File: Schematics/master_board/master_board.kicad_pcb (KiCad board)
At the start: 2 copper layers, 70 parts, among them J1 2x5x1.27mm, J10 Conn_01x06_Male, J11 Conn_01x06_Male, J12 Conn_01x06_Male, J13 Conn_01x06_Male, J14 Conn_01x06_Male, J15 Conn_01x06_Male, J16 Conn_01x06_Male, J17 Conn_01x06_Male, J18 Conn_01x06_Male, J19 Conn_01x06_Male, J2 USB_C_Receptacle_USB2.0, J20 Conn_01x06_Male, J21 Conn_01x06_Male, J22 Conn_01x06_Male, J23 Conn_01x06_Male, J24 Conn_01x06_Male, J25 Conn_01x06_Male, J26 Conn_01x06_Male, J3 Conn_01x01_Female, J4 Conn_01x01_Female, J5 Conn_01x01_Female, J6 Conn_01x01_Female, J7 Conn_01x06_Male, J8 Conn_01x06_Male, J9 Conn_01x06_Male, SW1 SW_Push, SW2 SW_Push, SW3 SW_Push, U1 NCP1117-3.3_SOT223, U2 RP2040, U3 W25Q16JVSSIQ, U4 74HCT154PW,118, U5 74HCT154PW,118, Y1 ABLS-12.000MHZ-B4-T

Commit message: Finalize master board placement, begin routing
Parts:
- added H1: MountingHole, MountingHole:MountingHole_3.2mm_M3, F.Cu at (22.0, 23.0)
- added H2: MountingHole, MountingHole:MountingHole_3.2mm_M3, F.Cu at (22.0, 169.0)
- added H3: MountingHole, MountingHole:MountingHole_3.2mm_M3, F.Cu at (168.0, 23.0)
- added H4: MountingHole, MountingHole:MountingHole_3.2mm_M3, F.Cu at (168.0, 169.0)
- moved U4 186.9 mm to (50.0, 40.0)
- moved U5 180.4 mm to (70.0, 40.0)
- moved J10 179.3 mm to (32.0, 146.8)
- moved J9 172.4 mm to (32.0, 115.2)
- moved J7 169.8 mm to (32.0, 52.2)
- moved R13 169.3 mm to (62.9, 21.9), turned to -90 degrees
- moved J8 169.2 mm to (32.0, 83.8)
- moved R15 165.0 mm to (63.6, 21.9), turned to 90 degrees
- moved C17 165.0 mm to (74.3, 21.7), turned to 90 degrees
- moved J14 164.7 mm to (63.5, 146.8)
- moved U3 162.8 mm to (68.9, 24.1)
- moved J13 157.3 mm to (63.5, 115.2)
- moved J11 154.4 mm to (63.5, 52.2)
- moved J12 153.7 mm to (63.5, 83.8)
- moved D1 151.2 mm to (82.7, 28.4), turned to 90 degrees
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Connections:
- net Net-(C13-Pad2) renamed /XTAL_OUT_PRE
- net Net-(J1-Pad10) renamed /CONN_RUN_N
- net Net-(J1-Pad2) renamed /CONN_SWDIO
- net Net-(J1-Pad4) renamed /CONN_SWCLK
- net Net-(J2-PadA5) renamed /CC1_USB
- net Net-(J2-PadB5) renamed /CC2_USB
- net Net-(J3-Pad1) renamed /CONN_HAP_L
- net Net-(J6-Pad1) renamed /CONN_HAP_R
- U2 pad 28: /GPIO17 -> /RESCAN_N
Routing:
- net /USB_D+: track 0.00 -> 32.3 mm, vias 0 -> 2
- net /USB_D-: track 0.00 -> 30.9 mm
- net /XTAL_OUT_PRE: track 0.00 -> 7.64 mm
- net /USB_D+I: track 0.00 -> 2.78 mm
- net /USB_D-I: track 0.00 -> 2.66 mm
- net +3V3: track 0.00 -> 1.85 mm
- net +1V1: track 0.00 -> 1.57 mm
- added copper zone on F.Cu, net +3V3
- added copper zone on B.Cu, net GND
- added copper zone on F.Cu, net GND
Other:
- board outline added: 156 x 156 mm

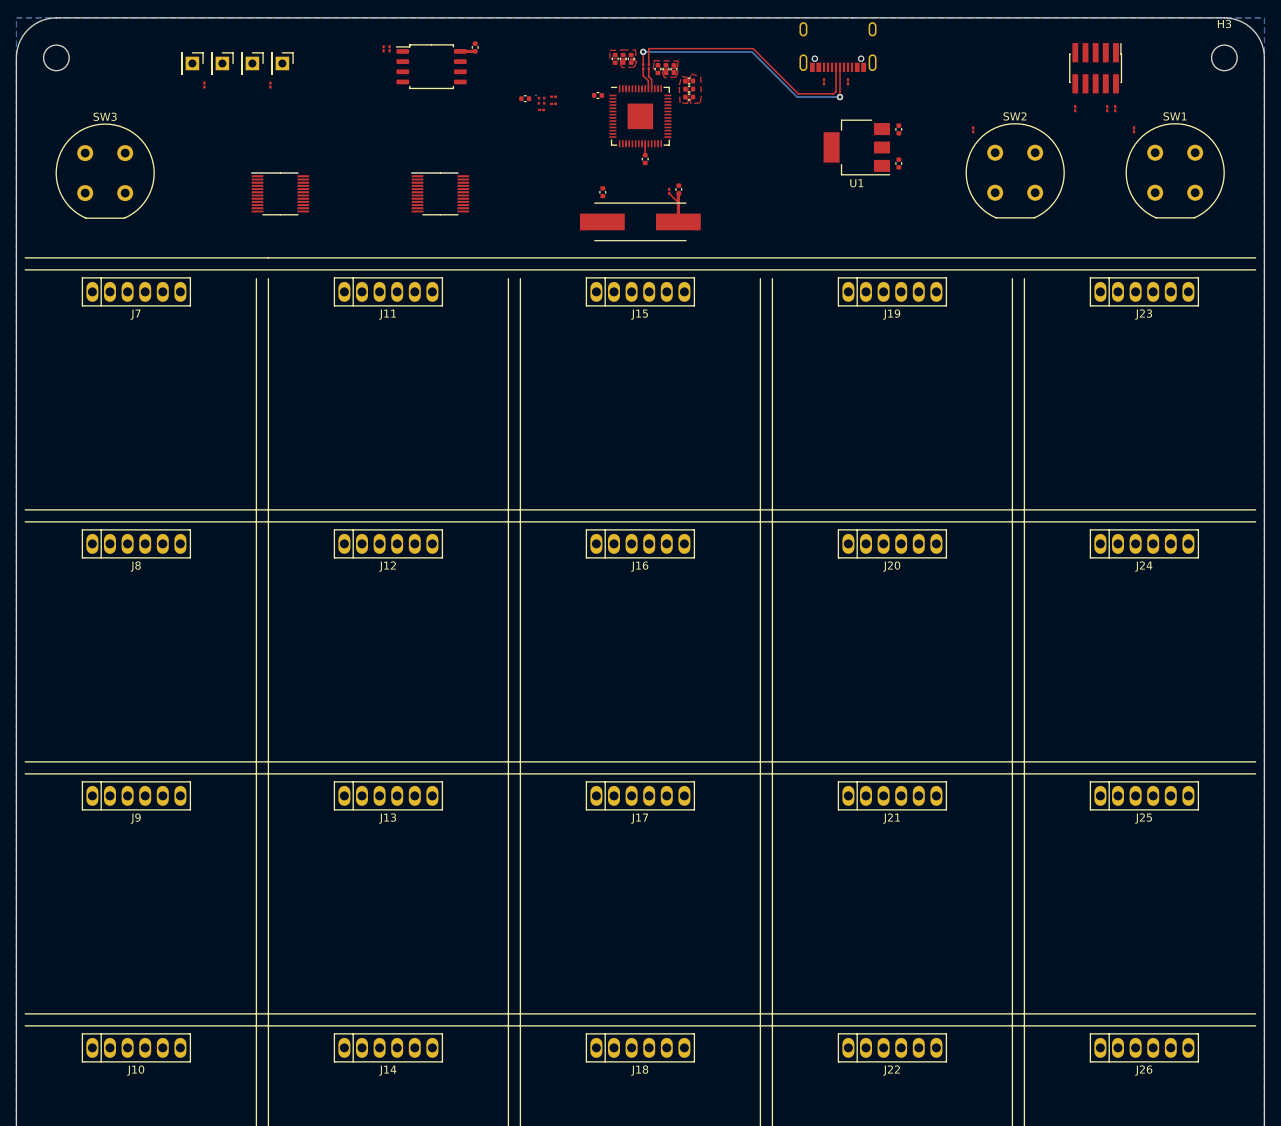
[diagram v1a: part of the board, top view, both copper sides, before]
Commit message: Route master board and DRC
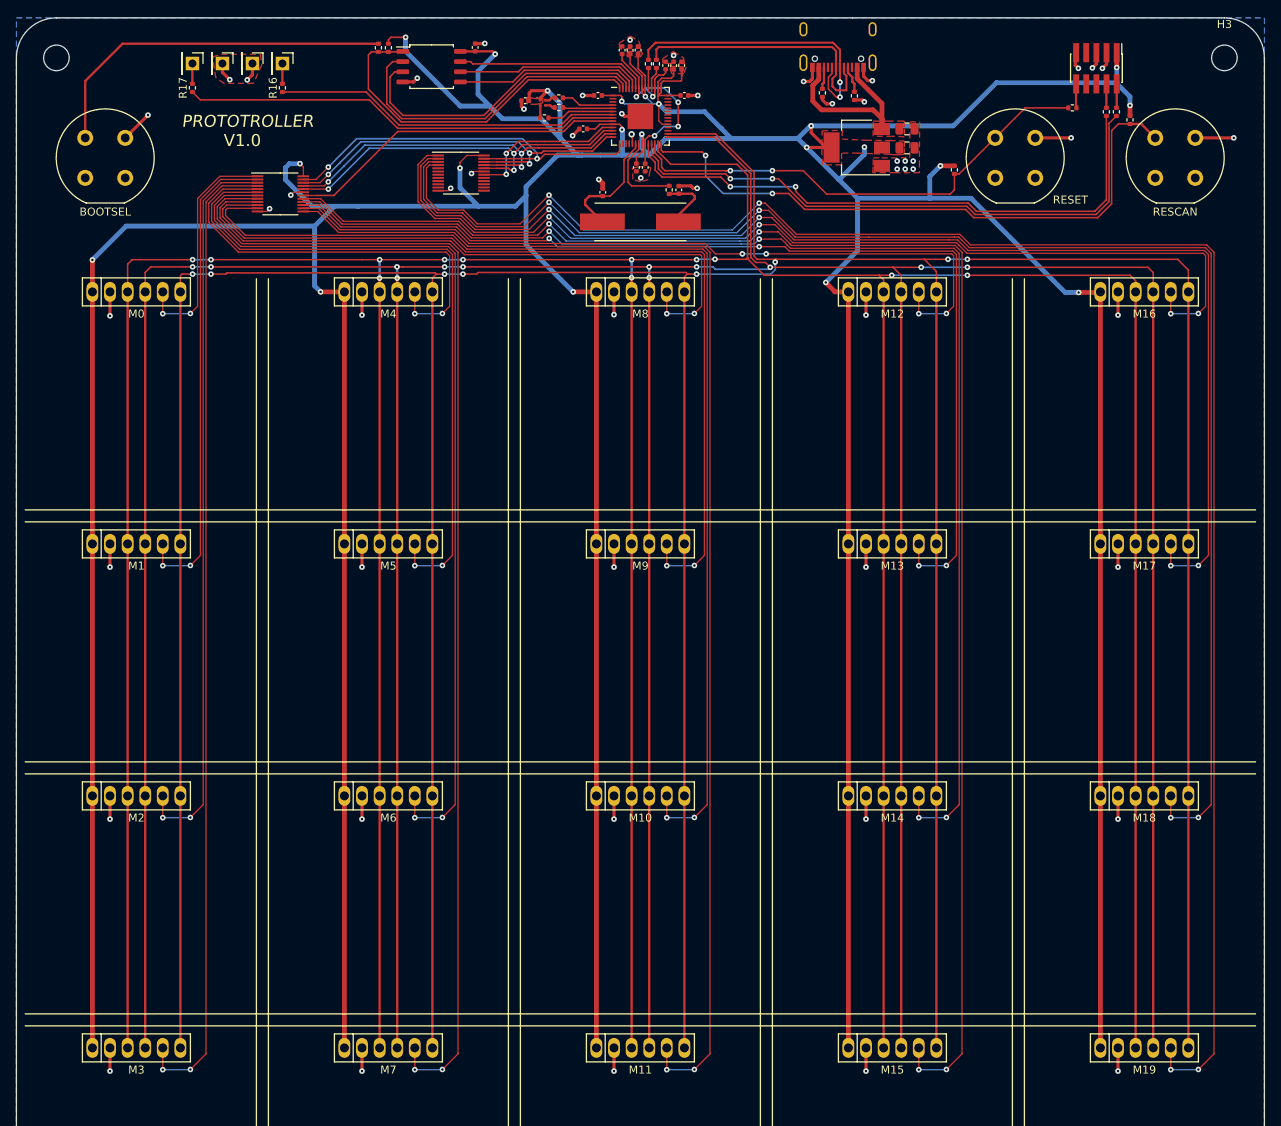
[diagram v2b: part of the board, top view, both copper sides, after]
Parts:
- C1, C2: footprint Capacitor_SMD:C_0402_1005Metric -> Capacitor_SMD:C_0805_2012Metric
- R1, R10, R11, R12, R13, R14, R15, R16, R17, R2, R3, R4, R5, R6, R7, R8, R9: footprint Resistor_SMD:R_01005_0402Metric -> Resistor_SMD:R_0402_1005Metric
- moved C11 13.8 mm to (87.8, 31.9), turned to 180 degrees
- moved C10 11.8 mm to (94.5, 36.7), turned to -90 degrees
- moved R12 5.52 mm to (134.2, 37.0)
- moved U5 3.67 mm to (72.6, 37.4)
- moved C2 2.20 mm to (128.3, 34.2), turned to 180 degrees
- moved R7 1.92 mm to (121.8, 27.8)
- moved BOOTSEL 1.90 mm to (25.6, 33.0)
- moved C9 1.90 mm to (100.5, 27.7)
- moved RESCAN 1.86 mm to (159.3, 33.0)
- moved RESET 1.86 mm to (139.3, 33.0)
- moved R16 1.54 mm to (50.2, 26.8)
- moved R17 1.54 mm to (39.0, 26.8), turned to 90 degrees
- moved R8 1.39 mm to (117.8, 27.4)
- moved C15 1.38 mm to (93.7, 22.0)
- moved C16 1.38 mm to (94.7, 22.0)
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- renumbered SW3 to BOOTSEL, J7 to M0, J8 to M1, J17 to M10, J18 to M11, J19 to M12, J20 to M13, J21 to M14, J22 to M15, J23 to M16, J24 to M17, J25 to M18, J26 to M19, J9 to M2, J10 to M3, J11 to M4, J12 to M5, J13 to M6, J14 to M7, J15 to M8, J16 to M9, SW1 to RESCAN, SW2 to RESET
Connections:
- M0 pad 2: /5-to-32/SPI_CSN0 -> GND
- M0 pad 3: SPI0_TX -> SPI0_RX
- M0 pad 4: SPI0_RX -> SPI0_SCLK
- M0 pad 5: SPI0_SCLK -> /5-to-32/SPI_CSN0
- M0 pad 6: GND -> SPI0_TX
- M1 pad 2: /5-to-32/SPI_CSN1 -> GND
- M1 pad 3: SPI0_TX -> SPI0_RX
- M1 pad 4: SPI0_RX -> SPI0_SCLK
- M1 pad 5: SPI0_SCLK -> /5-to-32/SPI_CSN1
- M1 pad 6: GND -> SPI0_TX
- M10 pad 2: /5-to-32/SPI_CSN10 -> GND
- M10 pad 3: SPI0_TX -> SPI0_RX
- M10 pad 4: SPI0_RX -> SPI0_SCLK
- M10 pad 5: SPI0_SCLK -> /5-to-32/SPI_CSN10
- M10 pad 6: GND -> SPI0_TX
- M11 pad 2: /5-to-32/SPI_CSN11 -> GND
- M11 pad 3: SPI0_TX -> SPI0_RX
- M11 pad 4: SPI0_RX -> SPI0_SCLK
- M11 pad 5: SPI0_SCLK -> /5-to-32/SPI_CSN11
- M11 pad 6: GND -> SPI0_TX
- M12 pad 2: /5-to-32/SPI_CSN12 -> GND
- M12 pad 3: SPI0_TX -> SPI0_RX
- M12 pad 4: SPI0_RX -> SPI0_SCLK
- M12 pad 5: SPI0_SCLK -> /5-to-32/SPI_CSN12
- M12 pad 6: GND -> SPI0_TX
- M13 pad 2: /5-to-32/SPI_CSN13 -> GND
- M13 pad 3: SPI0_TX -> SPI0_RX
- M13 pad 4: SPI0_RX -> SPI0_SCLK
- M13 pad 5: SPI0_SCLK -> /5-to-32/SPI_CSN13
- M13 pad 6: GND -> SPI0_TX
- M14 pad 2: /5-to-32/SPI_CSN14 -> GND
- M14 pad 3: SPI0_TX -> SPI0_RX
- M14 pad 4: SPI0_RX -> SPI0_SCLK
- M14 pad 5: SPI0_SCLK -> /5-to-32/SPI_CSN14
- M14 pad 6: GND -> SPI0_TX
- M15 pad 2: /5-to-32/SPI_CSN15 -> GND
- M15 pad 3: SPI0_TX -> SPI0_RX
- M15 pad 4: SPI0_RX -> SPI0_SCLK
- M15 pad 5: SPI0_SCLK -> /5-to-32/SPI_CSN15
- M15 pad 6: GND -> SPI0_TX
- M16 pad 2: /5-to-32/SPI_CSN16 -> GND
- M16 pad 3: SPI0_TX -> SPI0_RX
- M16 pad 4: SPI0_RX -> SPI0_SCLK
- M16 pad 5: SPI0_SCLK -> /5-to-32/SPI_CSN16
- M16 pad 6: GND -> SPI0_TX
- M17 pad 2: /5-to-32/SPI_CSN17 -> GND
- M17 pad 3: SPI0_TX -> SPI0_RX
- M17 pad 4: SPI0_RX -> SPI0_SCLK
- M17 pad 5: SPI0_SCLK -> /5-to-32/SPI_CSN17
- M17 pad 6: GND -> SPI0_TX
- M18 pad 2: /5-to-32/SPI_CSN18 -> GND
- M18 pad 3: SPI0_TX -> SPI0_RX
- M18 pad 4: SPI0_RX -> SPI0_SCLK
- M18 pad 5: SPI0_SCLK -> /5-to-32/SPI_CSN18
- M18 pad 6: GND -> SPI0_TX
- M19 pad 2: /5-to-32/SPI_CSN19 -> GND
- M19 pad 3: SPI0_TX -> SPI0_RX
- M19 pad 4: SPI0_RX -> SPI0_SCLK
- M19 pad 5: SPI0_SCLK -> /5-to-32/SPI_CSN19
- M19 pad 6: GND -> SPI0_TX
- M2 pad 2: /5-to-32/SPI_CSN2 -> GND
- M2 pad 3: SPI0_TX -> SPI0_RX
- M2 pad 4: SPI0_RX -> SPI0_SCLK
- M2 pad 5: SPI0_SCLK -> /5-to-32/SPI_CSN2
- M2 pad 6: GND -> SPI0_TX
- M3 pad 2: /5-to-32/SPI_CSN3 -> GND
- M3 pad 3: SPI0_TX -> SPI0_RX
- M3 pad 4: SPI0_RX -> SPI0_SCLK
- M3 pad 5: SPI0_SCLK -> /5-to-32/SPI_CSN3
- M3 pad 6: GND -> SPI0_TX
- M4 pad 2: /5-to-32/SPI_CSN4 -> GND
- M4 pad 3: SPI0_TX -> SPI0_RX
- M4 pad 4: SPI0_RX -> SPI0_SCLK
- M4 pad 5: SPI0_SCLK -> /5-to-32/SPI_CSN4
- M4 pad 6: GND -> SPI0_TX
- M5 pad 2: /5-to-32/SPI_CSN5 -> GND
- M5 pad 3: SPI0_TX -> SPI0_RX
- M5 pad 4: SPI0_RX -> SPI0_SCLK
- M5 pad 5: SPI0_SCLK -> /5-to-32/SPI_CSN5
- M5 pad 6: GND -> SPI0_TX
- M6 pad 2: /5-to-32/SPI_CSN6 -> GND
- M6 pad 3: SPI0_TX -> SPI0_RX
- M6 pad 4: SPI0_RX -> SPI0_SCLK
- M6 pad 5: SPI0_SCLK -> /5-to-32/SPI_CSN6
- M6 pad 6: GND -> SPI0_TX
- M7 pad 2: /5-to-32/SPI_CSN7 -> GND
- M7 pad 3: SPI0_TX -> SPI0_RX
- M7 pad 4: SPI0_RX -> SPI0_SCLK
- M7 pad 5: SPI0_SCLK -> /5-to-32/SPI_CSN7
- M7 pad 6: GND -> SPI0_TX
- M8 pad 2: /5-to-32/SPI_CSN8 -> GND
- M8 pad 3: SPI0_TX -> SPI0_RX
- M8 pad 4: SPI0_RX -> SPI0_SCLK
- M8 pad 5: SPI0_SCLK -> /5-to-32/SPI_CSN8
- M8 pad 6: GND -> SPI0_TX
- M9 pad 2: /5-to-32/SPI_CSN9 -> GND
- M9 pad 3: SPI0_TX -> SPI0_RX
- M9 pad 4: SPI0_RX -> SPI0_SCLK
- M9 pad 5: SPI0_SCLK -> /5-to-32/SPI_CSN9
- M9 pad 6: GND -> SPI0_TX
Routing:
- net +3V3: track 1.85 -> 876.6 mm, vias 0 -> 21
- net SPI0_TX: track 0.00 -> 641.4 mm, vias 0 -> 8
- net SPI0_SCLK: track 0.00 -> 639.6 mm, vias 0 -> 12
- net SPI0_RX: track 0.00 -> 639.0 mm, vias 0 -> 12
- net /5-to-32/SPI_CSN19: track 0.00 -> 221.5 mm, vias 0 -> 4
- net /5-to-32/SPI_CSN15: track 0.00 -> 196.3 mm, vias 0 -> 4
- net /5-to-32/SPI_CSN18: track 0.00 -> 189.5 mm, vias 0 -> 4
- net /5-to-32/SPI_CSN14: track 0.00 -> 163.2 mm, vias 0 -> 4
- net /5-to-32/SPI_CSN11: track 0.00 -> 162.1 mm, vias 0 -> 2
- net /5-to-32/SPI_CSN17: track 0.00 -> 157.6 mm, vias 0 -> 4
- net /5-to-32/SPI_CSN7: track 0.00 -> 147.9 mm, vias 0 -> 2
- net /5-to-32/SPI_CSN10: track 0.00 -> 144.2 mm, vias 0 -> 2
- net /5-to-32/SPI_CSN13: track 0.00 -> 130.0 mm, vias 0 -> 4
- net /5-to-32/SPI_CSN16: track 0.00 -> 125.7 mm, vias 0 -> 4
- net /5-to-32/SPI_CSN3: track 0.00 -> 122.7 mm, vias 0 -> 2
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- added copper zone on F.Cu, net VBUS
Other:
- board text added: "PROTOTROLLER"
- board text added: "V1.0"
- board text added: "Yu-yang Hsieh (Leo) Caleb O'Malley Britton McLeavy Merrick Ryman Evan Zhang"

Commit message: Master board finishing touches
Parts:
- moved R16 11.4 mm to (38.9, 26.7)
- moved J3 11.4 mm to (38.9, 23.7)
- moved R17 11.3 mm to (50.3, 26.7)
- moved J6 11.3 mm to (50.3, 23.7)
- renumbered RESCAN to SW1, RESET to SW2, BOOTSEL to SW3
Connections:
- U2 pad 7: /HAP_L -> /HAP_R
- U2 pad 8: /HAP_R -> /HAP_L
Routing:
- net /HAP_L: track 43.6 -> 55.5 mm
- net /HAP_R: track 55.0 -> 43.8 mm
- net /BOOTSEL_N: track 45.7 -> 44.8 mm
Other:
- board text added: "BOOTSEL"
- board text added: "GND"
- board text added: "HAPTIC L"
- board text added: "HAPTIC R"
- board text added: "M3"
- board text added: "ON"
- board text added: "RESCAN"
- board text added: "RESET"
- board text added: "REV A"
- board text added: "SWD"
- board text added: "USB"
- board text added: "Yu-yang Hsieh (Leo) Caleb O'Malley Britton McLeavy Merrick Ryman Evan Zhang Made with <3"
- board text removed: "V1.0"
- board text removed: "Yu-yang Hsieh (Leo) Caleb O'Malley Britton McLeavy Merrick Ryman Evan Zhang"

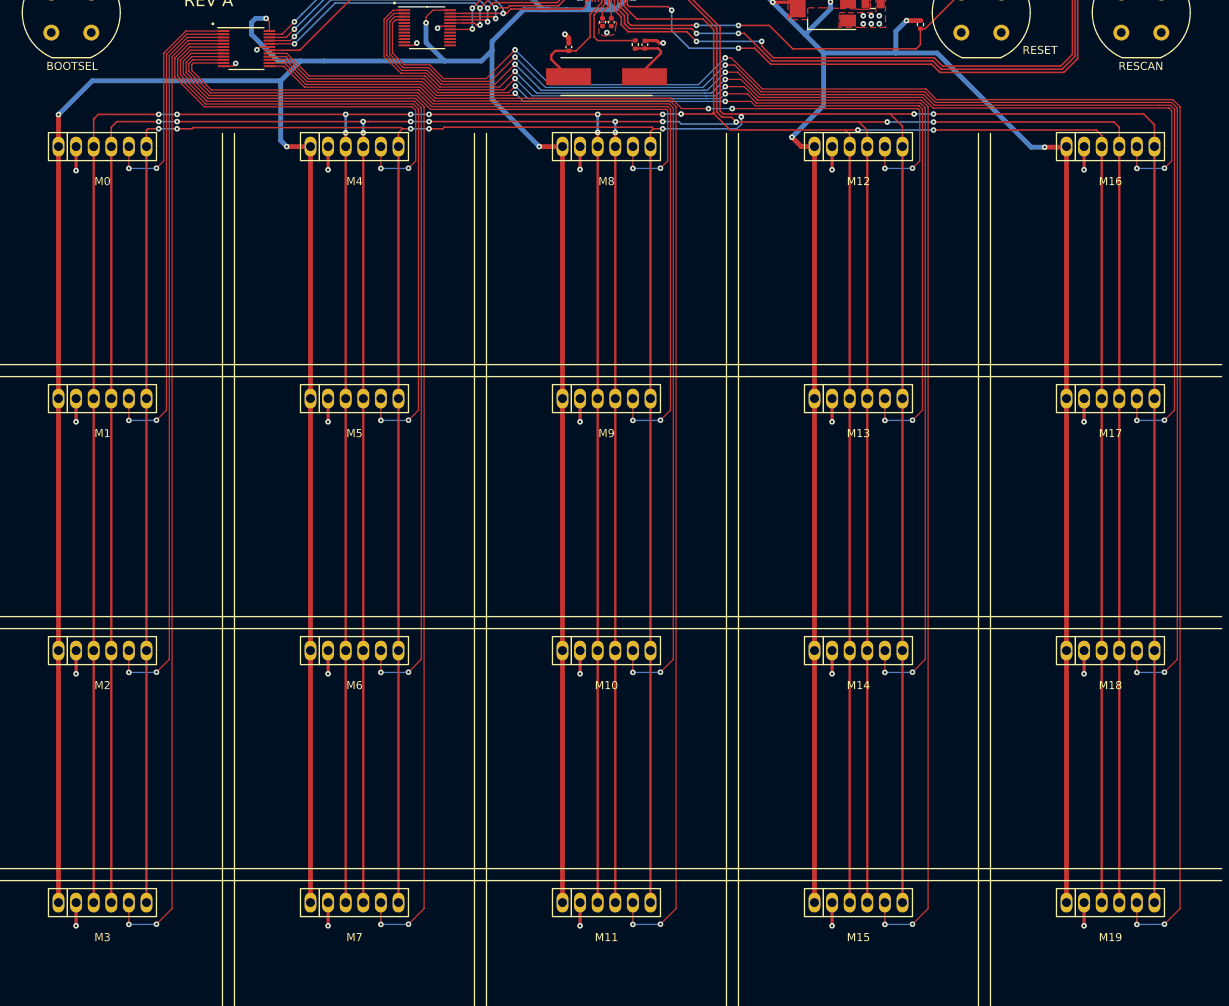
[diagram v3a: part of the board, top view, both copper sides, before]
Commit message: Modified .gitignore, shifted all master_board pogo-pins down 1.5mm
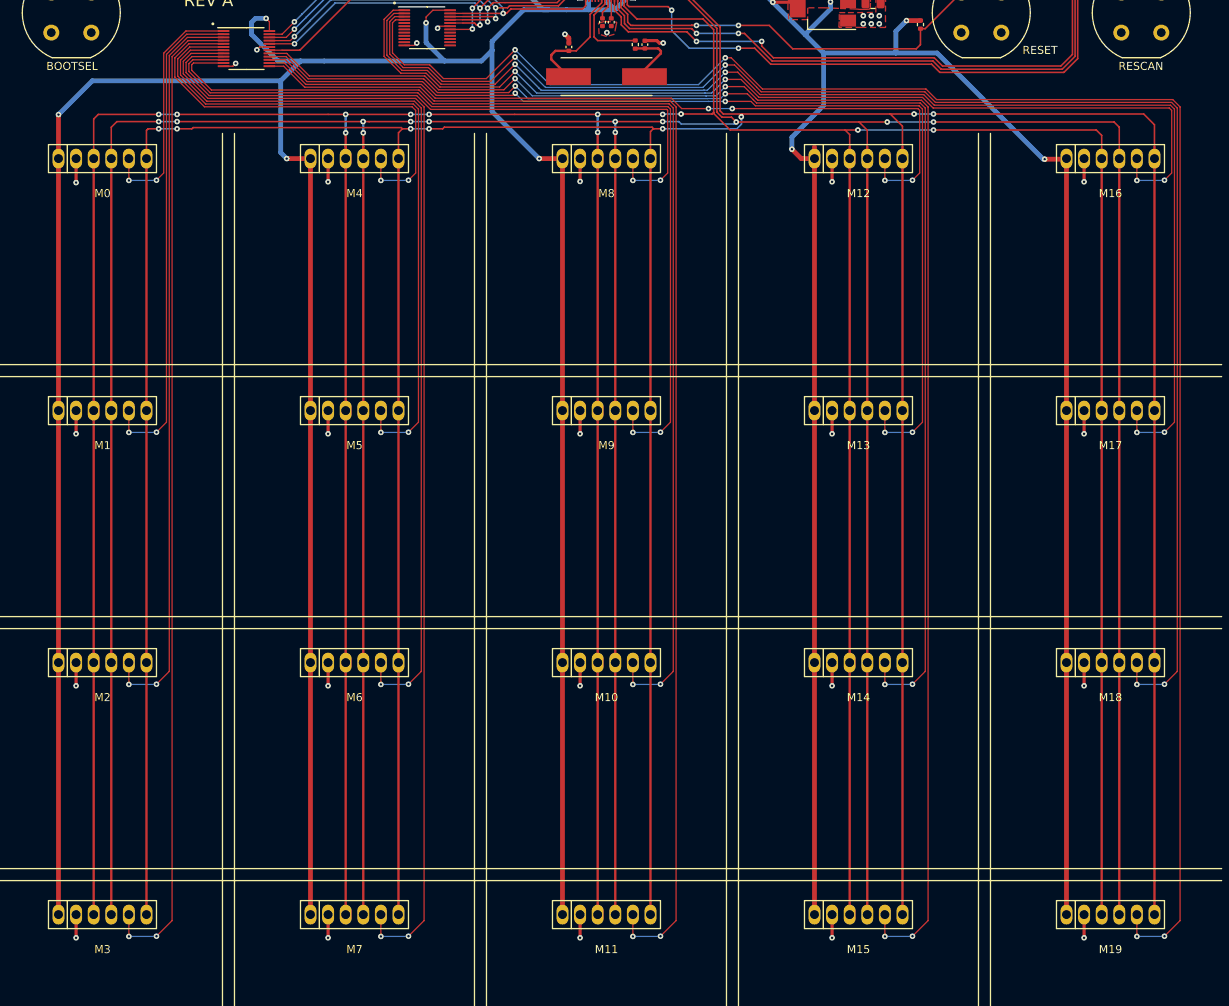
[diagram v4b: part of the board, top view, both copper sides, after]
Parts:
- moved M0 1.50 mm to (32.0, 53.8)
- moved M1 1.50 mm to (32.0, 85.2)
- moved M10 1.50 mm to (95.0, 116.8)
- moved M11 1.50 mm to (95.0, 148.2)
- moved M12 1.50 mm to (126.5, 53.8)
- moved M13 1.50 mm to (126.5, 85.2)
- moved M14 1.50 mm to (126.5, 116.8)
- moved M15 1.50 mm to (126.5, 148.2)
- moved M16 1.50 mm to (158.0, 53.8)
- moved M17 1.50 mm to (158.0, 85.2)
- moved M18 1.50 mm to (158.0, 116.8)
- moved M19 1.50 mm to (158.0, 148.2)
- moved M2 1.50 mm to (32.0, 116.8)
- moved M3 1.50 mm to (32.0, 148.2)
- moved M4 1.50 mm to (63.5, 53.8)
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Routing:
- net +3V3: track 876.6 -> 884.6 mm
- net SPI0_RX: track 639.0 -> 646.5 mm
- net SPI0_SCLK: track 639.6 -> 647.1 mm
- net SPI0_TX: track 641.4 -> 648.9 mm
- net /5-to-32/SPI_CSN7: track 147.9 -> 149.4 mm
- net /5-to-32/SPI_CSN11: track 162.1 -> 163.6 mm
- net /5-to-32/SPI_CSN5: track 85.8 -> 87.3 mm
- net /5-to-32/SPI_CSN12: track 97.5 -> 99.0 mm
- net /5-to-32/SPI_CSN9: track 113.2 -> 114.7 mm
- net /5-to-32/SPI_CSN8: track 82.2 -> 83.7 mm
- net /5-to-32/SPI_CSN6: track 116.9 -> 118.4 mm
- net /5-to-32/SPI_CSN4: track 54.8 -> 56.3 mm
- net /5-to-32/SPI_CSN3: track 122.7 -> 124.2 mm
- net /5-to-32/SPI_CSN2: track 91.6 -> 93.1 mm
- net /5-to-32/SPI_CSN19: track 221.5 -> 223.0 mm
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
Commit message: Final improvements
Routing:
- net +3V3: track 884.6 -> 883.8 mm, vias 21 -> 16
- net SPI0_RX: vias 12 -> 11
- net SPI0_SCLK: vias 12 -> 11
